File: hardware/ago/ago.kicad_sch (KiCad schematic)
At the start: 17 parts

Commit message: fix hardware design.
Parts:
- removed U?: STM32F103C4Tx - MainController, Package_QFP:LQFP-48_7x7mm_P0.5mm, symbol MCU_ST_STM32F1:STM32F103C4Tx
- added U?: STM32F103C8Tx, Package_QFP:LQFP-48_7x7mm_P0.5mm, symbol MCU_ST_STM32F1:STM32F103C8Tx
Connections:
- net at U?.10 (IN3): now also U?.30 (PA9)
- net at U?.12 (IN4): now also U?.29 (PA8)
- net at U?.19 (IN5): now also U?.28 (PB15)
- net at U?.20 (IN6): now also U?.27 (PB14)
- net at U?.22 (IN7): now also U?.26 (PB13)
- net at U?.23 (IN8): now also U?.25 (PB12)
- net at U?.6 (IN2): now also U?.31 (PA10)
- net at U?.7 (IN1): now also U?.32 (PA11)

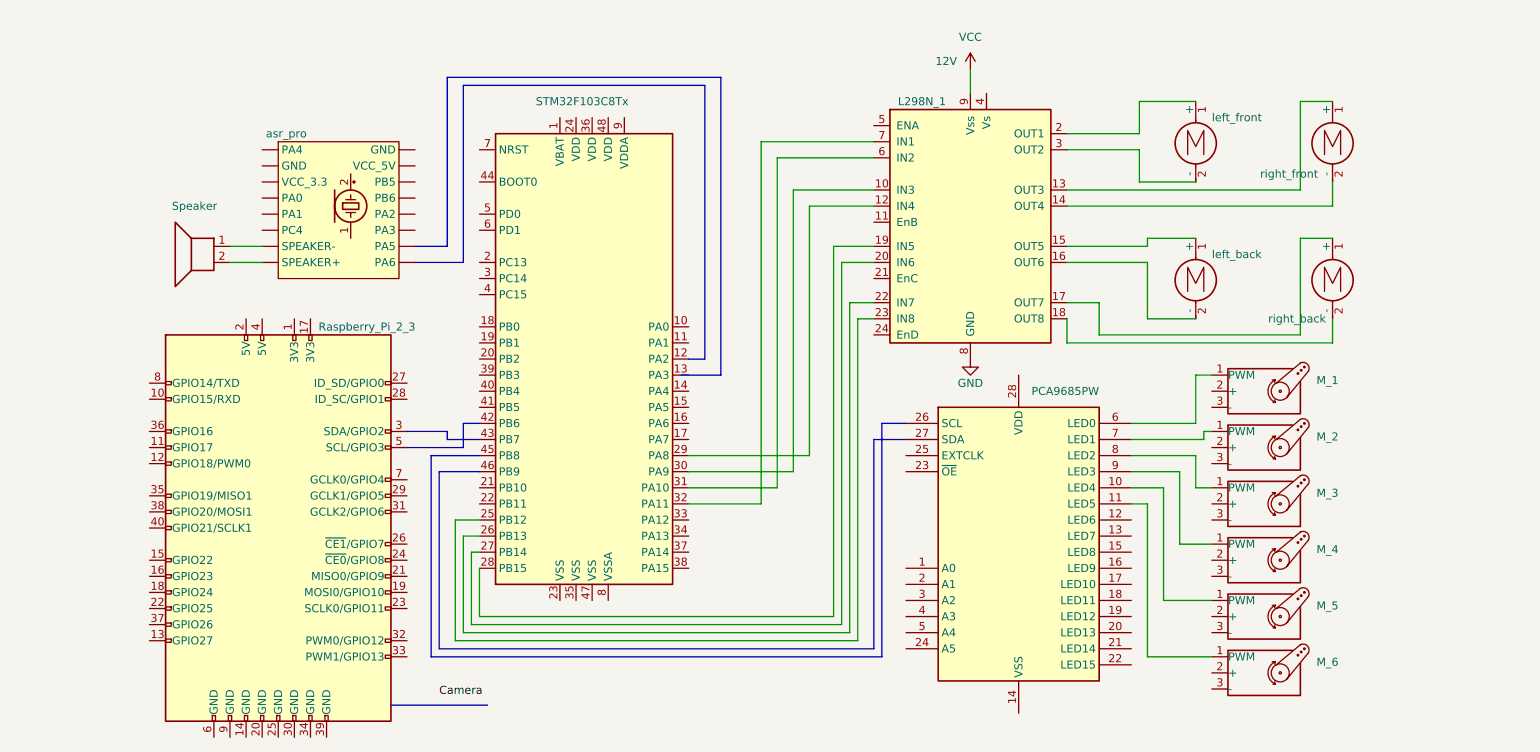
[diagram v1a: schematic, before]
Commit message: redesign hardware architechure.
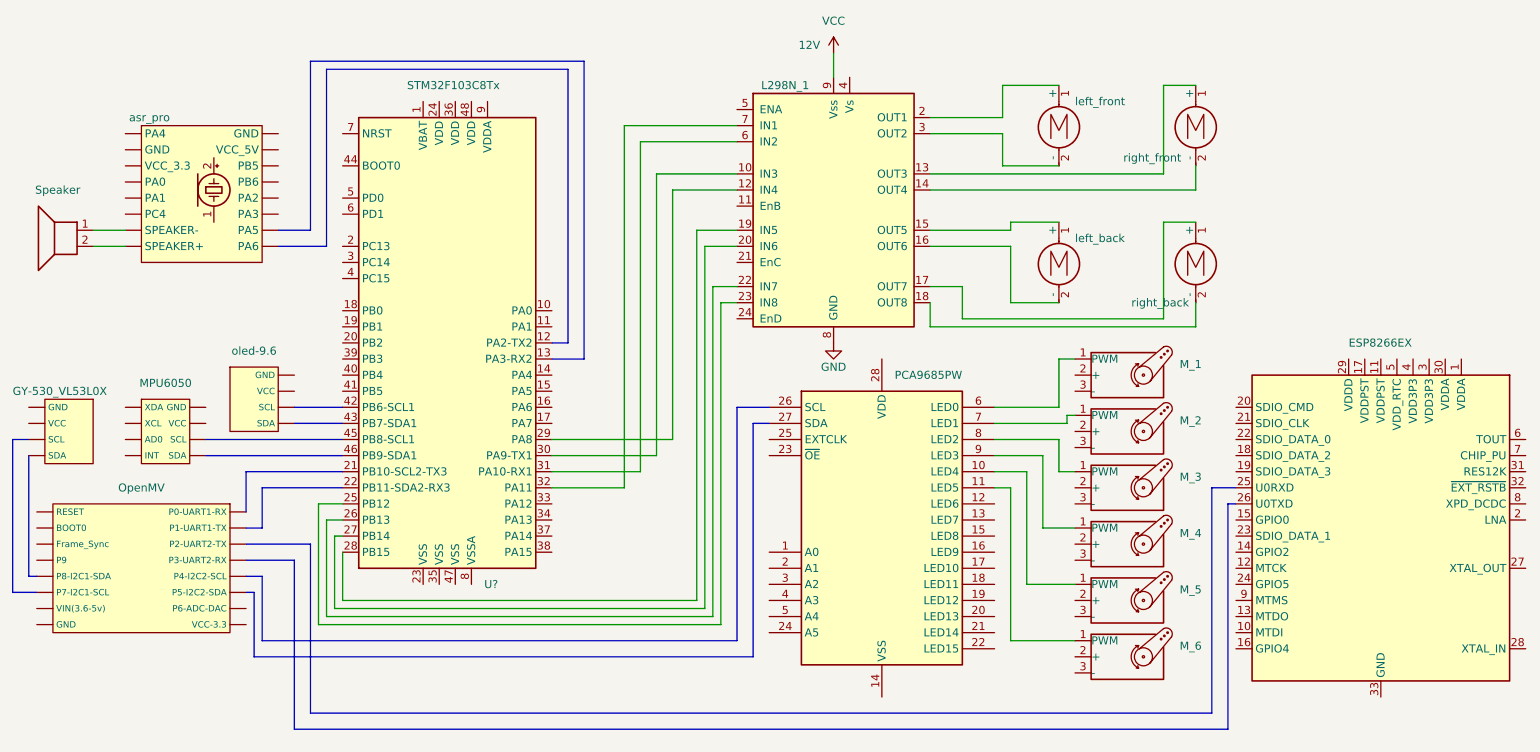
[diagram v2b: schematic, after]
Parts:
- removed J?: Raspberry_Pi_2_3, symbol Connector:Raspberry_Pi_2_3
- removed U?: STM32F103C8Tx, Package_QFP:LQFP-48_7x7mm_P0.5mm, symbol MCU_ST_STM32F1:STM32F103C8Tx
- added U?: OpenMV, symbol Video:OpenMV
- added U?: ESP8266EX, Package_DFN_QFN:QFN-32-1EP_5x5mm_P0.5mm_EP3.45x3.45mm, symbol MCU_Espressif:ESP8266EX
- added U?: oled-9.6, symbol Display_Graphic:oled-9.6
- added U?: MPU6050, symbol Display_Graphic:MPU6050
- added U?: GY-530_VL53L0X, symbol Video:GY-530_VL53L0X
- added U?: STM32F103C8Tx, Package_QFP:LQFP-48_7x7mm_P0.5mm, symbol MCU_ST_STM32F1:STM32F103C8Tx
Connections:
- net at U?.10 (IN3): now also U?.30 (PA9-TX1)
- net at U?.12 (IN4): now also U?.29 (PA8)
- net at U?.19 (IN5): now also U?.28 (PB15)
- net at U?.20 (IN6): now also U?.27 (PB14)
- net at U?.22 (IN7): now also U?.26 (PB13)
- net at U?.23 (IN8): now also U?.25 (PB12)
- net at U?.6 (IN2): now also U?.31 (PA10-RX1)
- net at U?.7 (IN1): now also U?.32 (PA11)
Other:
- moved on the sheet: M_1, M_2, M_3, M_4, M_5, M_6, left_back, left_front, right_back, right_front

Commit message: fix connection of esp8266.
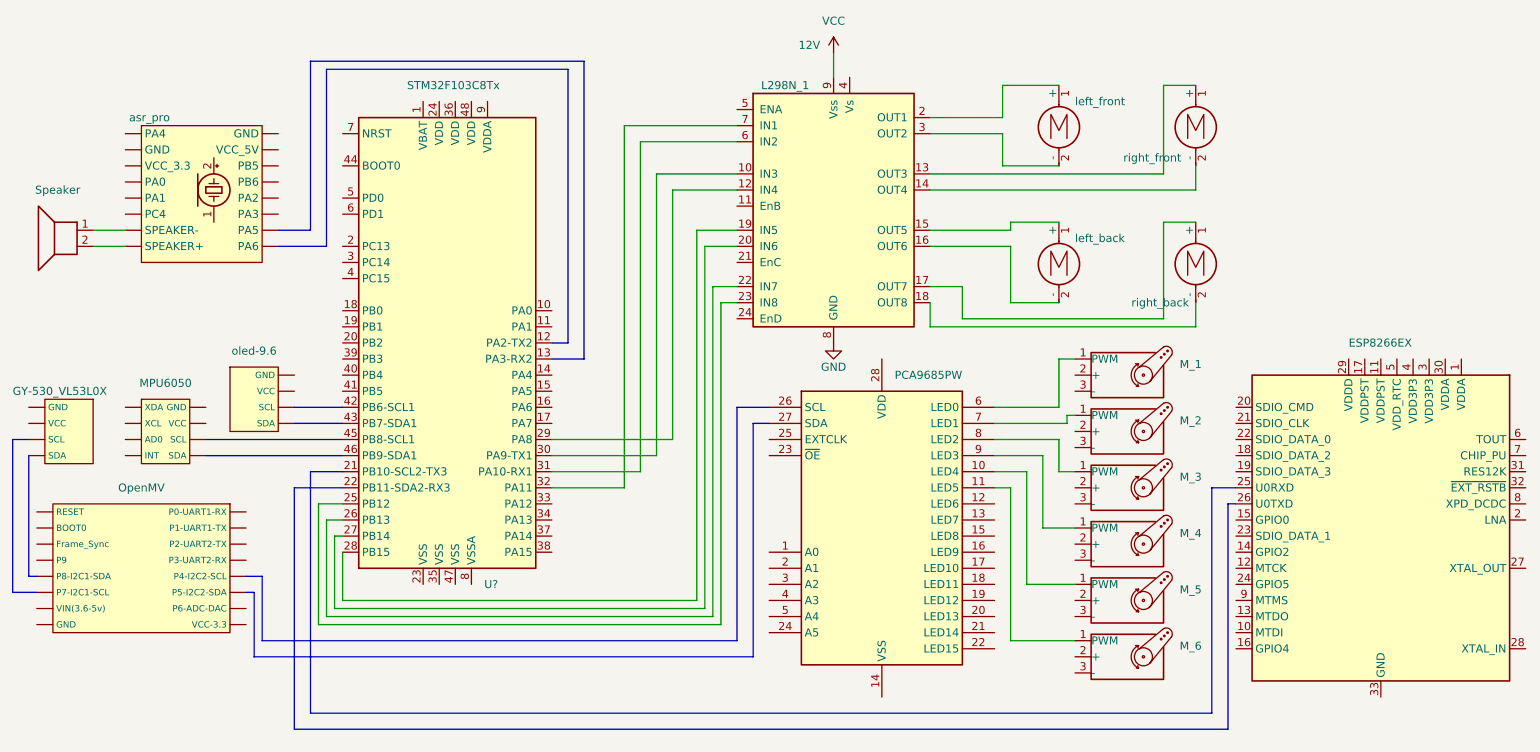
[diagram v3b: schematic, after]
